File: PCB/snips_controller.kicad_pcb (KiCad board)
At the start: 4 copper layers, 40 x 115 mm, 66 parts

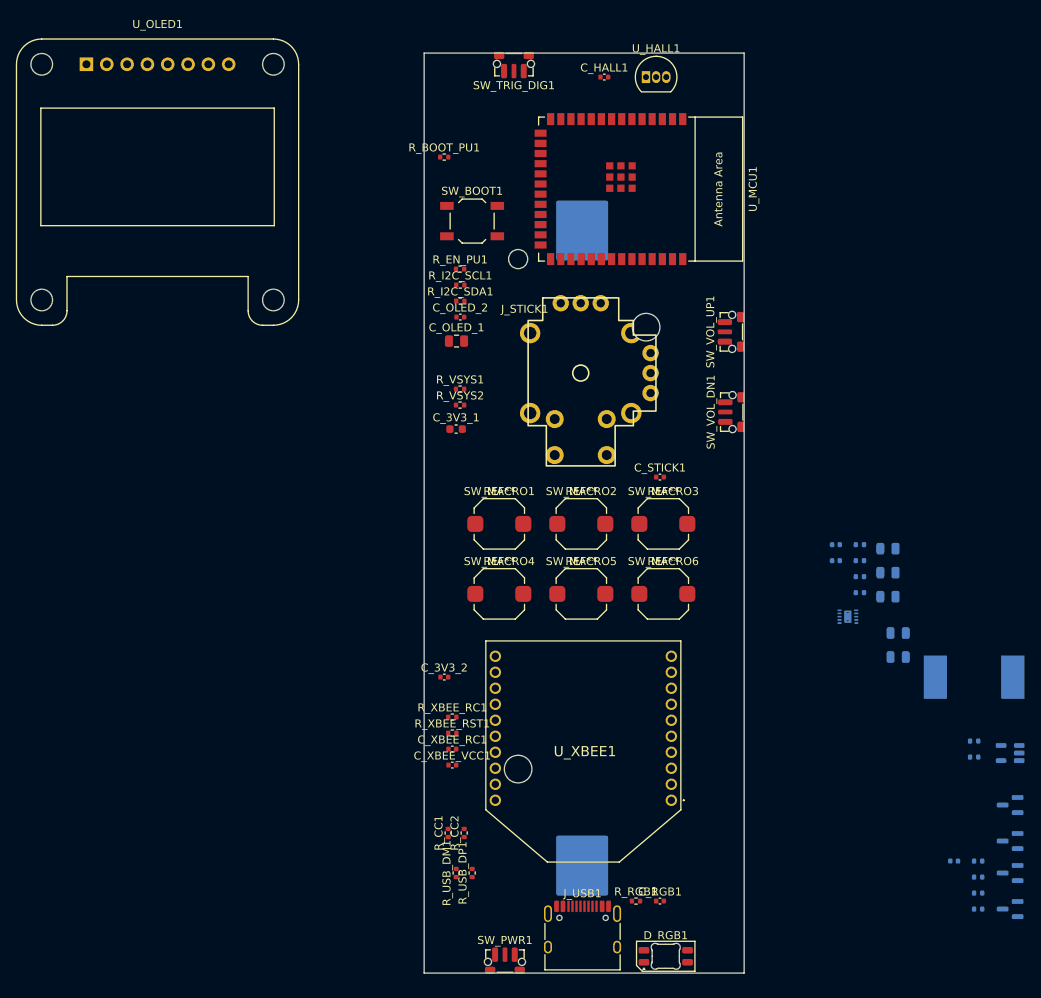
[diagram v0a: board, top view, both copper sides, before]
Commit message: refactor: swap footprints and add symmetry
This updates the footprints of a couple components to be smaller and closer to what we want. It also adds two buttons to ensure left and right side symmetry.
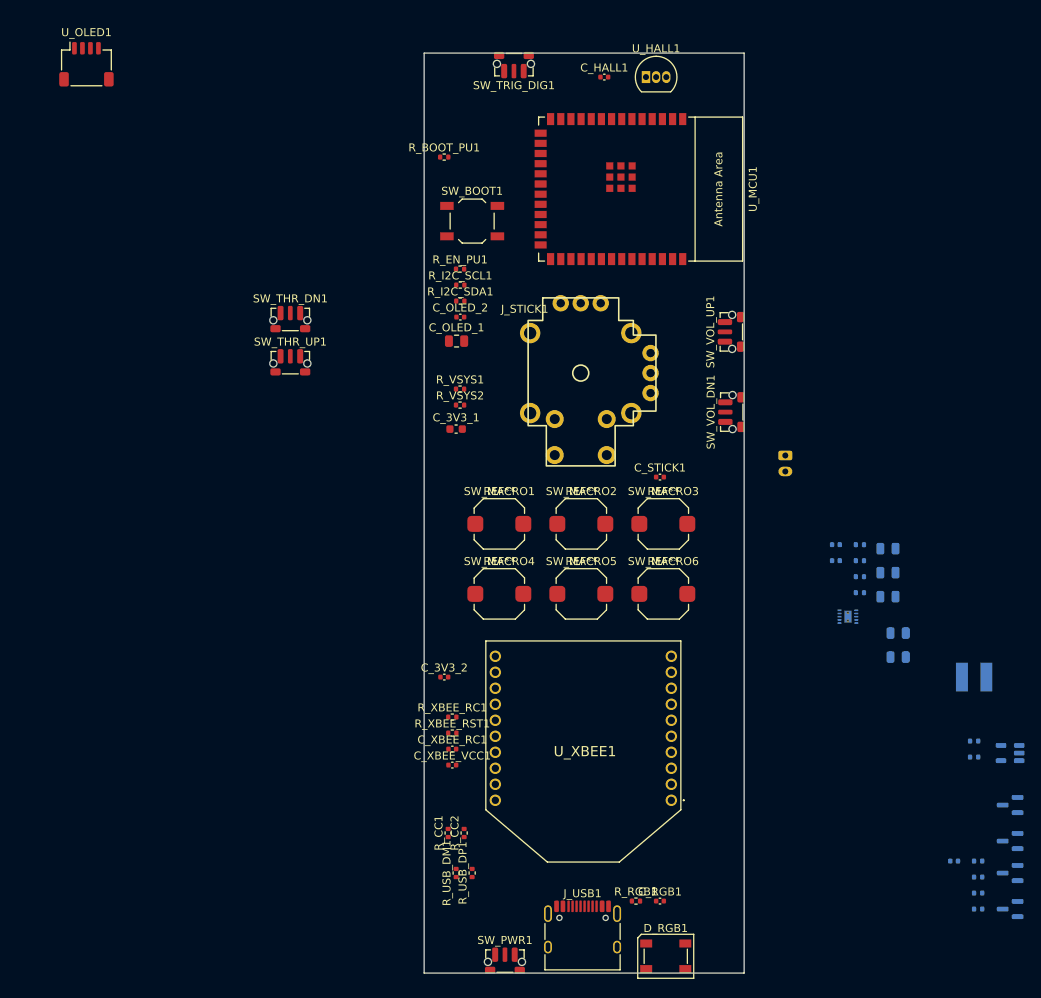
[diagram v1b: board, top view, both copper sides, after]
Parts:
- added SW_THR_DN1: Alps_SKRTLAE010, Button_Switch_SMD:SW_Push_1P1T-MP_NO_Horizontal_Alps_SKRTLAE010, F.Cu at (97.3, 78.4)
- added SW_THR_UP1: Alps_SKRTLAE010, Button_Switch_SMD:SW_Push_1P1T-MP_NO_Horizontal_Alps_SKRTLAE010, F.Cu at (97.3, 83.8)
- BT1: value Li-ion_18650_or_14500 -> JST-PH_2Pin_Battery; footprint Battery:BatteryHolder_Keystone_1042_1x18650 -> Connector_JST:JST_PH_S2B-PH-K_1x02_P2.00mm_Horizontal
- D_RGB1: value SK6812 -> SK6812MINI-E; footprint LED_SMD:LED_SK6812MINI-E_3.2x2.8mm_P1.5mm_ReverseMount -> LED_SMD:LED_SK6812_PLCC4_5.0x5.0mm_P3.2mm
- L_BUCK1: value 1µH -> 2.2µH; footprint Inductor_SMD:L_Bourns_SRR1260 -> Inductor_SMD:L_Bourns-SRN4018
- SW_MACRO1, SW_MACRO2, SW_MACRO3, SW_MACRO4, SW_MACRO5, SW_MACRO6: value Omron_B3F -> 6x6x5mm SMD Tactile
- SW_PWR1, SW_TRIG_DIG1, SW_VOL_DN1, SW_VOL_UP1: value Omron_B3F -> Alps_SKRTLAE010
- U_OLED1: value SSD1306_1.3in -> JST-SH_4Pin_OLED; footprint Display:Adafruit_SSD1306 -> Connector_JST:JST_SH_SM04B-SRSS-TB_1x04-1MP_P1.00mm_Horizontal
- moved BT1 27.9 mm to (159.2, 95.3)
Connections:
- U_MCU1 pad 32: unconnected-(U_MCU1-MTCK/GPIO39/CLK_OUT3/SUBSPICS1-Pad32) -> /Buttons_Direct/BTN_THR_UP
- U_MCU1 pad 33: unconnected-(U_MCU1-MTDO/GPIO40/CLK_OUT2-Pad33) -> /Buttons_Direct/BTN_THR_DN

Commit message: layout: everything is on the board
The board edge cuts are down to 100mm x 35mm. All the components have the right footprints and are on the board, but no traces exist yet, and not all circuits are laid out properly yet. Lots of DRC warnings.
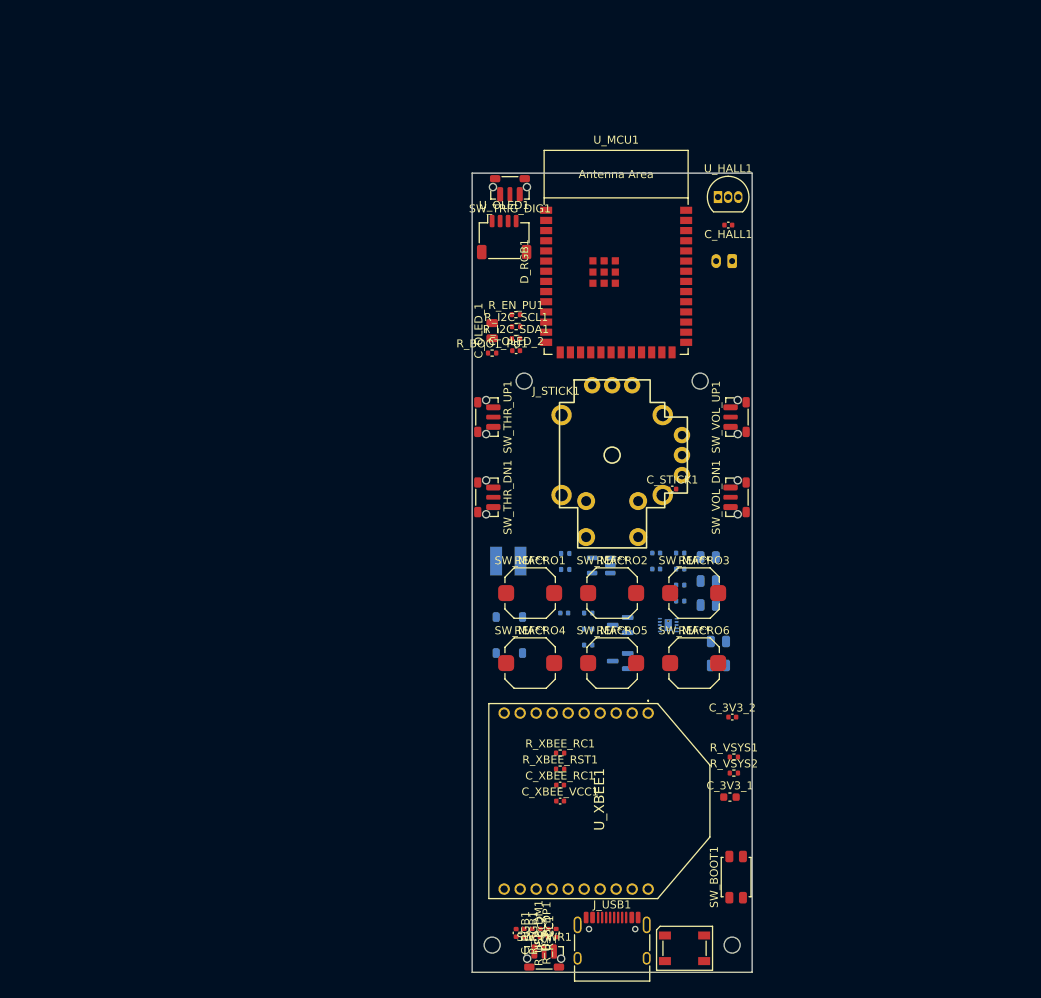
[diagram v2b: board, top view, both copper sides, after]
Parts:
- added MHole: MountingHole_2mm, MountingHole:MountingHole_2mm, F.Cu at (126.5, 86.0)
- added MHole: MountingHole_2mm, MountingHole:MountingHole_2mm, F.Cu at (148.5, 86.0)
- added MHole: MountingHole_2mm, MountingHole:MountingHole_2mm, F.Cu at (122.5, 156.5)
- added MHole: MountingHole_2mm, MountingHole:MountingHole_2mm, F.Cu at (152.5, 156.5)
- D_OR1, D_OR2: footprint Package_TO_SOT_SMD:SOT-23 -> Diode_SMD:D_SOD-123
- SW_BOOT1: value TP-1221U-K9K5325 -> Panasonic_EVQP2; footprint Button_Switch_SMD:SW_SPST_TL3342 -> Button_Switch_SMD:SW_SPST_EVQP2_ShortPushTravel_H2.1mm
- moved SW_BOOT1 88.4 mm to (153.0, 148.0), turned to 90 degrees
- moved D_OR1 66.9 mm to (124.7, 115.5)
- moved D_OR2 66.9 mm to (124.7, 120.0)
- moved L_BUCK1 60.0 mm to (124.5, 108.5)
- moved C_DBNC1 57.8 mm to (131.5, 115.0)
- moved Q_LATCH1 57.8 mm to (138.5, 116.5)
- moved Q_PWR1 57.8 mm to (138.5, 121.0)
- moved R_BTN_PU1 57.8 mm to (134.5, 115.0)
- moved R_GATE1 57.8 mm to (134.5, 117.0)
- moved R_LATCH_G1 57.8 mm to (134.5, 119.0)
- moved R_PWR_SENSE1 57.8 mm to (134.5, 121.0)
- moved R_VSYS1 57.3 mm to (152.7, 133.0)
- moved R_VSYS2 57.3 mm to (152.7, 135.0)
- moved C_3V3_1 57.3 mm to (152.2, 138.0)
- moved U_OLED1 56.5 mm to (124.0, 68.0)
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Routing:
- added copper zone on In1.Cu, net 3V3
- added copper zone on In2.Cu, net GND
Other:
- board size 40 x 115 mm -> 35 x 99.9 mm

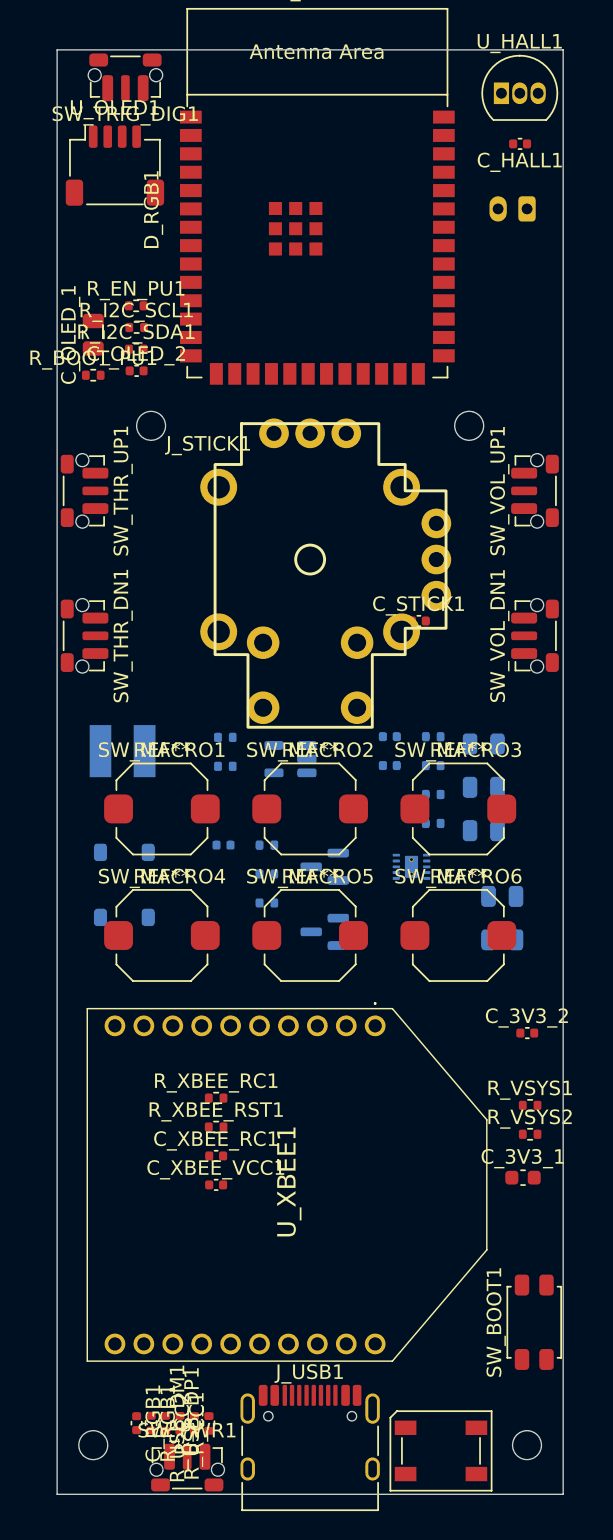
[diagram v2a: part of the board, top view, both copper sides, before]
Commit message: refactor: tracing and diagrams
Adding traces and laying out circuits for the buck, planning for the power and charging circuits.
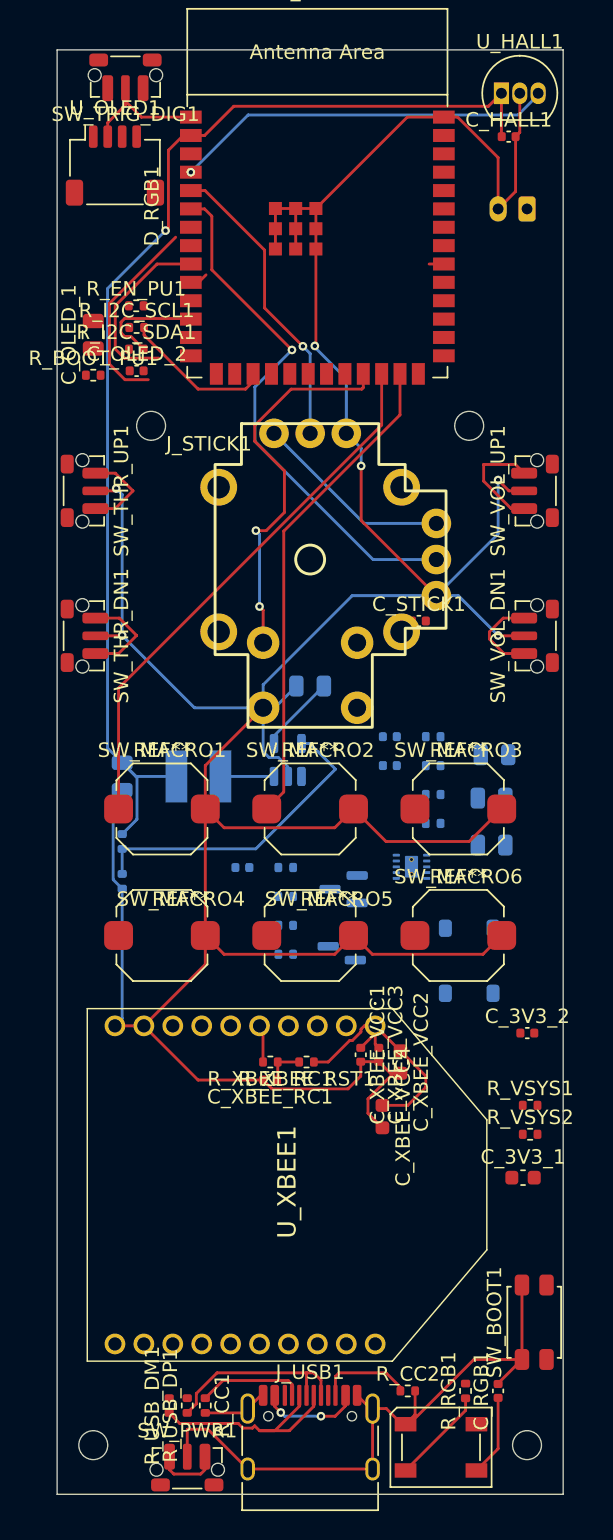
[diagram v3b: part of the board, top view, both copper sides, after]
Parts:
- added C_XBEE_VCC2: 1µF, Capacitor_SMD:C_0603_1608Metric, F.Cu at (143.8, 130.0)
- added C_XBEE_VCC3: 47pF, Capacitor_SMD:C_0402_1005Metric, F.Cu at (142.2, 129.5)
- added C_XBEE_VCC4: 10µF, Capacitor_SMD:C_0603_1608Metric, F.Cu at (142.5, 133.8)
- moved C_BUCK_OUT1 28.6 mm to (124.5, 110.2), turned to -90 degrees
- moved C_RGB1 25.1 mm to (150.5, 152.8), turned to 90 degrees
- moved D_OR1 24.4 mm to (148.5, 120.8)
- moved D_OR2 24.4 mm to (148.5, 125.2)
- moved R_RGB1 21.9 mm to (148.2, 152.8), turned to 90 degrees
- moved C_BUCK_IN1 19.7 mm to (137.5, 104.0)
- moved R_CC2 16.9 mm to (144.2, 152.8), turned to 0 degrees
- moved C_XBEE_VCC1 13.5 mm to (141.0, 129.5), turned to -90 degrees
- moved R_FB2 10.7 mm to (124.5, 117.5), turned to -90 degrees
- moved R_FB1 10.1 mm to (124.5, 114.8), turned to 90 degrees
- moved R_XBEE_RST1 7.70 mm to (137.2, 130.0), turned to 180 degrees
- moved C_XBEE_RC1 6.44 mm to (134.7, 131.2), turned to 180 degrees
- moved L_BUCK1 5.53 mm to (129.8, 110.2)
- moved R_XBEE_RC1 4.51 mm to (134.8, 130.0), turned to 180 degrees
- moved R_USB_DM1 2.14 mm to (127.8, 153.8)
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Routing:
- net GND: track 0.00 -> 312.7 mm, vias 0 -> 6
- net 3V3: track 0.00 -> 119.8 mm, vias 0 -> 1
- net /Buttons_Direct/BTN_MACRO1: track 0.00 -> 37.6 mm
- net /MCU_Core/STICK_Y: track 0.00 -> 36.5 mm, vias 0 -> 1
- net /Buttons_Direct/BTN_MACRO2: track 0.00 -> 33.9 mm
- net /MCU_Core/BTN_STICK: track 0.00 -> 26.8 mm, vias 0 -> 2
- net /Hall_Trigger/TRIG_ANALOG: track 0.00 -> 26.4 mm, vias 0 -> 1
- net /Power_Buck/BUCK_FB: track 0.00 -> 21.8 mm
- net /Buttons_Direct/BTN_VOL_DN: track 0.00 -> 21.2 mm
- net /MCU_Core/STICK_X: track 0.00 -> 20.8 mm, vias 0 -> 1
- net /Buttons_Direct/BTN_VOL_UP: track 0.00 -> 20.5 mm
- net /MCU_Core/USB_DM: track 0.00 -> 16.3 mm
- net /MCU_Core/USB_DP: track 0.00 -> 13.6 mm
- net /MCU_Core/I2C_SCL: track 0.00 -> 10.4 mm
- net /MCU_Core/I2C_SDA: track 0.00 -> 7.73 mm
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
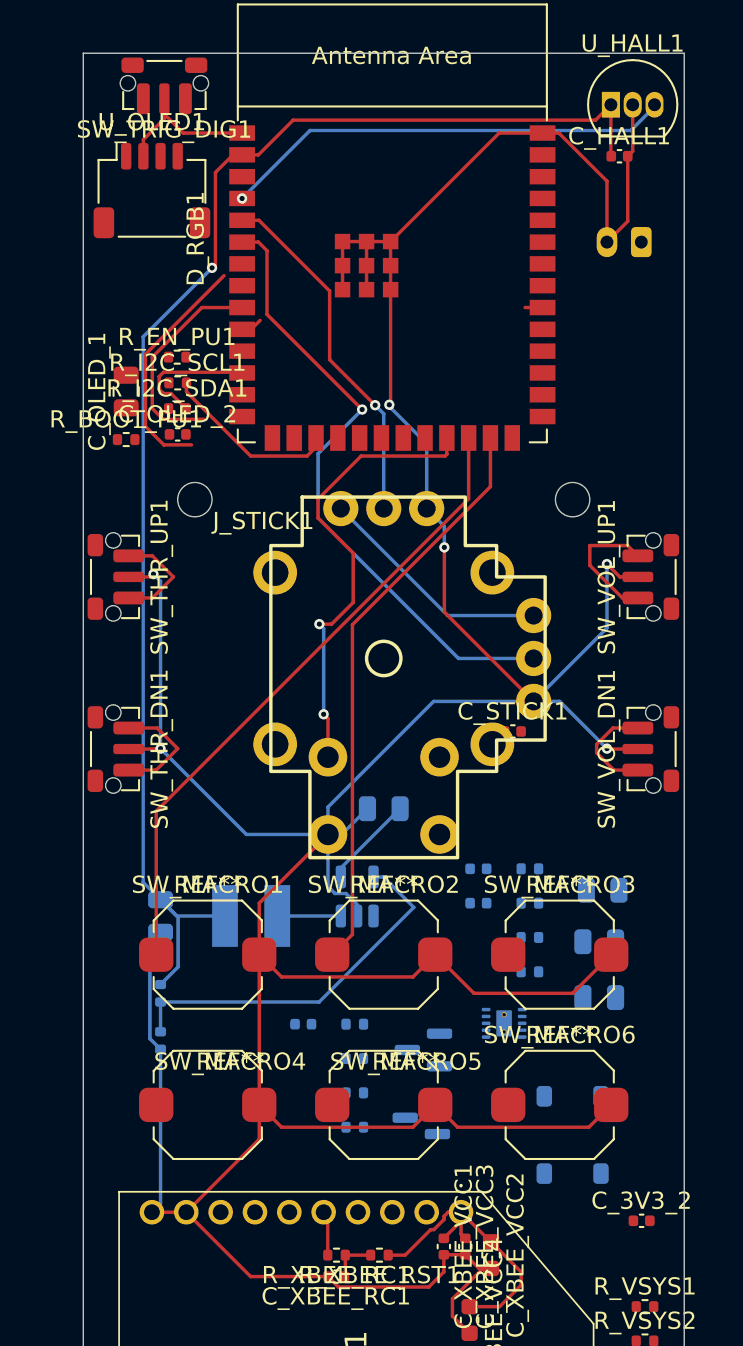
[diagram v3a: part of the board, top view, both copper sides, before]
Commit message: PCB cleanup (#21)
I always forget that I can just via into the ground or 3.3v plane and dont need a full trace.
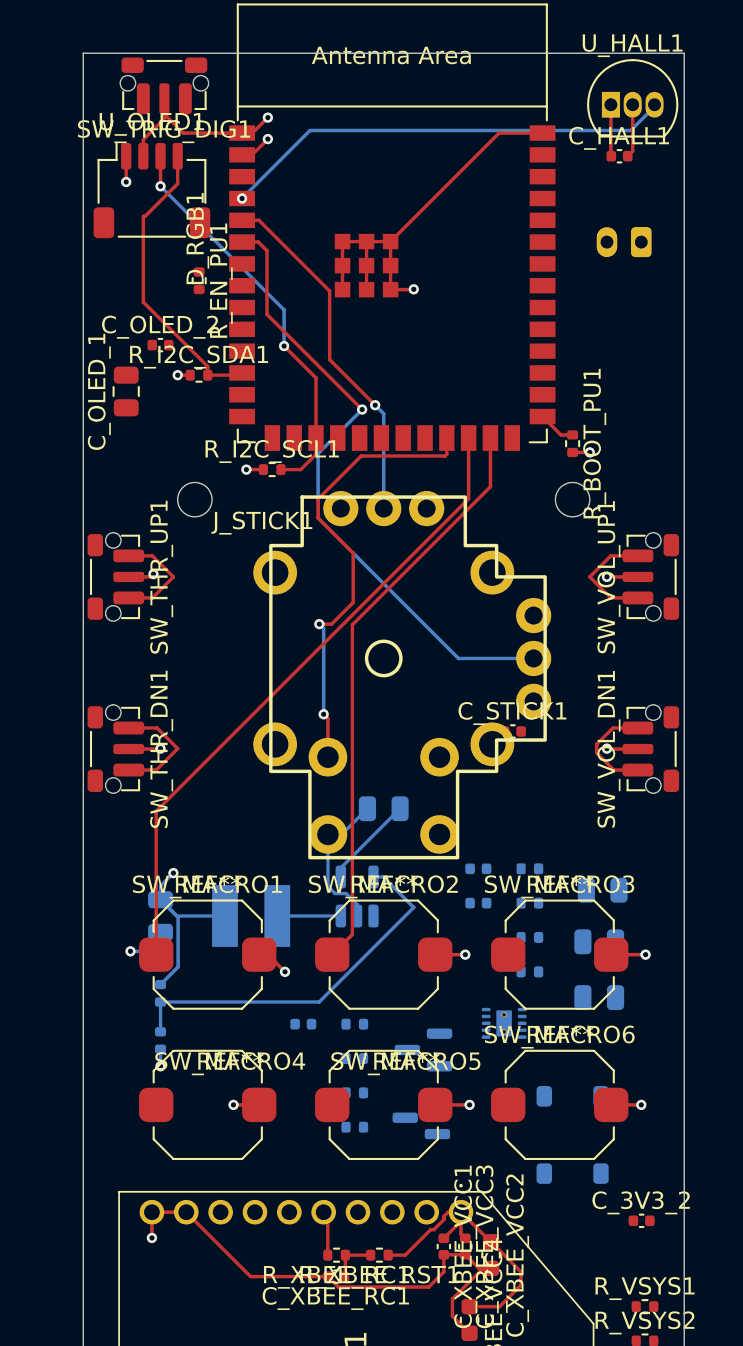
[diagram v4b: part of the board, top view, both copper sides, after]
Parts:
- moved R_BOOT_PU1 26.0 mm to (148.5, 82.7), turned to -90 degrees
- moved R_I2C_SCL1 7.47 mm to (131.0, 84.2)
- moved C_OLED_2 5.30 mm to (124.5, 77.0)
- moved R_EN_PU1 4.63 mm to (126.8, 73.2), turned to -90 degrees
- moved R_I2C_SDA1 2.32 mm to (126.7, 78.8)
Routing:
- net GND: track 312.7 -> 147.7 mm, vias 6 -> 15
- net 3V3: track 119.8 -> 44.9 mm, vias 1 -> 6
- net /Buttons_Direct/BTN_VOL_DN: track 21.2 -> 6.64 mm
- net /Buttons_Direct/BTN_VOL_UP: track 20.5 -> 6.61 mm
- net /MCU_Core/I2C_SCL: track 10.4 -> 23.5 mm, vias 0 -> 2
- net /MCU_Core/I2C_SDA: track 7.73 -> 17.3 mm
- net /MCU_Core/MCU_BOOT: track 0.00 -> 2.19 mm
- net /Buttons_Direct/BTN_THR_UP: track 7.23 -> 6.21 mm
